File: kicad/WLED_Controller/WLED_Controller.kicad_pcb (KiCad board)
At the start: 2 copper layers, 72 x 50 mm, 51 parts, among them J1 USB_C_Receptacle_USB2.0, J3 AudioJack, Q1 BC847, Q2 BC847, SW1 SW_RESET, SW2 SW_BOOT, SW3 SW_Push, SW4 SW_Push, SW5 SW_Push, SW6 SW_Push, SW7 SW_Push, U1 ESP32-WROOM-32, U2 CH340C, U3 NCP1117-3.3, U4 TSSP58P38

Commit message: begin creating schematic
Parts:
- removed C13, C14, C15, C16: 100n, Capacitor_SMD:C_0603_1608Metric_Pad1.08x0.95mm_HandSolder
- removed SW4, SW5, SW6, SW7: SW_Push, Button_Switch_THT:SW_PUSH_6mm_H13mm
- added J2: Conn_01x05, GioN_Custom:TerminalBlock_WAGO_236-405_1x05_P5.00mm_45Degree, F.Cu at (19.5, -9.40)
- added J5: Conn_01x05, GioN_Custom:TerminalBlock_WAGO_236-405_1x05_P5.00mm_45Degree, F.Cu at (9.40, -31.6)
- added J6: Conn_01x02, GioN_Custom:TerminalBlock_WAGO_236-402_1x02_P5.00mm_45Degree, F.Cu at (36.6, -40.6)
- added JP1: SolderJumper_3_Open, Jumper:SolderJumper-3_P1.3mm_Open_RoundedPad1.0x1.5mm_NumberLabels, F.Cu at (11.4, -5.59)
- added JP2: SolderJumper_2_Open, Jumper:SolderJumper-2_P1.3mm_Open_RoundedPad1.0x1.5mm, F.Cu at (28.6, -24.1)
- added JP3: SolderJumper_2_Open, Jumper:SolderJumper-2_P1.3mm_Open_RoundedPad1.0x1.5mm, F.Cu at (24.9, -16.5)
- added JP4: SolderJumper_3_Open, Jumper:SolderJumper-3_P1.3mm_Open_RoundedPad1.0x1.5mm_NumberLabels, F.Cu at (45.5, -11.2)
- added Q10: IRFL4105PBF, Package_TO_SOT_SMD:SOT-223, B.Cu at (38.4, -19.3)
- added Q3: IRFL4105PBF, Package_TO_SOT_SMD:SOT-223, B.Cu at (16.3, -19.3)
- added Q4: IRFL4105PBF, Package_TO_SOT_SMD:SOT-223, F.Cu at (18.8, -30.5)
- added Q5: IRFL4105PBF, Package_TO_SOT_SMD:SOT-223, F.Cu at (26.2, -30.5)
- added Q6: IRFL4105PBF, Package_TO_SOT_SMD:SOT-223, F.Cu at (33.5, -30.5)
- added Q7: IRFL4105PBF, Package_TO_SOT_SMD:SOT-223, F.Cu at (40.9, -30.5)
- added Q8: IRFL4105PBF, Package_TO_SOT_SMD:SOT-223, B.Cu at (23.6, -19.3)
- added Q9: IRFL4105PBF, Package_TO_SOT_SMD:SOT-223, B.Cu at (31.0, -19.3)
- added R13: 100R, Resistor_SMD:R_0603_1608Metric_Pad0.98x0.95mm_HandSolder, F.Cu at (11.4, 36.2)
- added R14: 100R, Resistor_SMD:R_0603_1608Metric_Pad0.98x0.95mm_HandSolder, F.Cu at (11.4, 38.7)
- added R16: 10k, Resistor_SMD:R_0603_1608Metric_Pad0.98x0.95mm_HandSolder, F.Cu at (11.4, 43.7)
- added R18: 10k, Resistor_SMD:R_0603_1608Metric_Pad0.98x0.95mm_HandSolder, F.Cu at (11.4, 48.7)
- added R20: 10k, Resistor_SMD:R_0603_1608Metric_Pad0.98x0.95mm_HandSolder, F.Cu at (15.7, 38.7)
- added R22: 10k, Resistor_SMD:R_0603_1608Metric_Pad0.98x0.95mm_HandSolder, F.Cu at (15.7, 43.7)
- added R23: 100R, Resistor_SMD:R_0603_1608Metric_Pad0.98x0.95mm_HandSolder, F.Cu at (15.7, 46.2)
- added R24: 100R, Resistor_SMD:R_0603_1608Metric_Pad0.98x0.95mm_HandSolder, F.Cu at (15.7, 48.7)
- added R25: 10k, Resistor_SMD:R_0603_1608Metric_Pad0.98x0.95mm_HandSolder, F.Cu at (20.1, 36.2)
- added R26: 10k, Resistor_SMD:R_0603_1608Metric_Pad0.98x0.95mm_HandSolder, F.Cu at (20.1, 38.7)
- added R27: 10k, Resistor_SMD:R_0603_1608Metric_Pad0.98x0.95mm_HandSolder, F.Cu at (20.1, 41.2)
- added R28: 10k, Resistor_SMD:R_0603_1608Metric_Pad0.98x0.95mm_HandSolder, F.Cu at (20.1, 43.7)
- R15, R17, R19, R21: value 10k -> 100R
- U2: moved to B.Cu
- moved C10 172.5 mm to (51.6, -43.1), turned to -90 degrees
- moved C11 170.8 mm to (49.3, -40.1)
- moved U3 169.2 mm to (56.1, -45.2), turned to 90 degrees
- moved C6 163.6 mm to (56.1, -37.8), turned to 180 degrees
- moved C7 161.2 mm to (56.1, -39.9), turned to 180 degrees
- moved C3 160.5 mm to (63.5, -39.9)
- moved SW1 156.9 mm to (63.2, -46.2), turned to -90 degrees
- moved C2 155.2 mm to (63.5, -37.6)
- moved C1 148.4 mm to (64.2, -35.6)
- moved SW3 146.6 mm to (42.5, -48.5)
- moved U4 139.3 mm to (69.9, -37.6), turned to 90 degrees
- moved D4 137.4 mm to (64.0, -2.40), turned to 90 degrees
- moved R11 136.7 mm to (64.0, -12.3), turned to -90 degrees
- moved R8 130.2 mm to (59.9, -12.3), turned to 90 degrees
- moved U2 128.5 mm to (55.8, -14.3), turned to 90 degrees
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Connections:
- net Button1 renamed Button0
- net CS renamed IO5
- net DTA/CTRL renamed IO25
- net MOSI renamed IO23
- net ON renamed IO22
- net RESET renamed IO4
- net SCLK renamed IO18
- net SENSE2 renamed IO26
- J3 pad 2: SENSE1 -> SENSE0
- R15 pad 1: +3.3V -> R1
- R15 pad 2: Button2 -> Net-(Q4-G)
- R17 pad 1: +3.3V -> G1
- R17 pad 2: Button3 -> Net-(Q5-G)
- R19 pad 1: +3.3V -> B1
- R19 pad 2: Button4 -> Net-(Q6-G)
- R21 pad 1: +3.3V -> W1
- R21 pad 2: Button5 -> Net-(Q7-G)
- U1 pad 13: SENSE1 -> IO14
- U1 pad 14: unconnected-(U1-IO12-Pad14) -> IO12
- U1 pad 16: Button5 -> IO13
- U1 pad 23: Button4 -> IO15
- U1 pad 27: Button3 -> IO16
- U1 pad 28: Button2 -> IO17
- U1 pad 33: unconnected-(U1-IO21-Pad33) -> IO21
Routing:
- net Net-(JP1-B): track 0.00 -> 46.8 mm
- net Net-(J5-Pin_4): track 0.00 -> 31.3 mm
- net Net-(J2-Pin_3): track 0.00 -> 23.8 mm
- net Net-(J5-Pin_3): track 0.00 -> 22.8 mm
- net Net-(J5-Pin_2): track 0.00 -> 17.2 mm
- net Net-(J2-Pin_2): track 0.00 -> 17.0 mm
- net Net-(J2-Pin_4): track 0.00 -> 13.2 mm
- net Net-(J5-Pin_5): track 0.00 -> 12.6 mm
- net Net-(J2-Pin_5): track 0.00 -> 11.7 mm
- net Net-(JP4-B): track 0.00 -> 10.7 mm, vias 0 -> 1

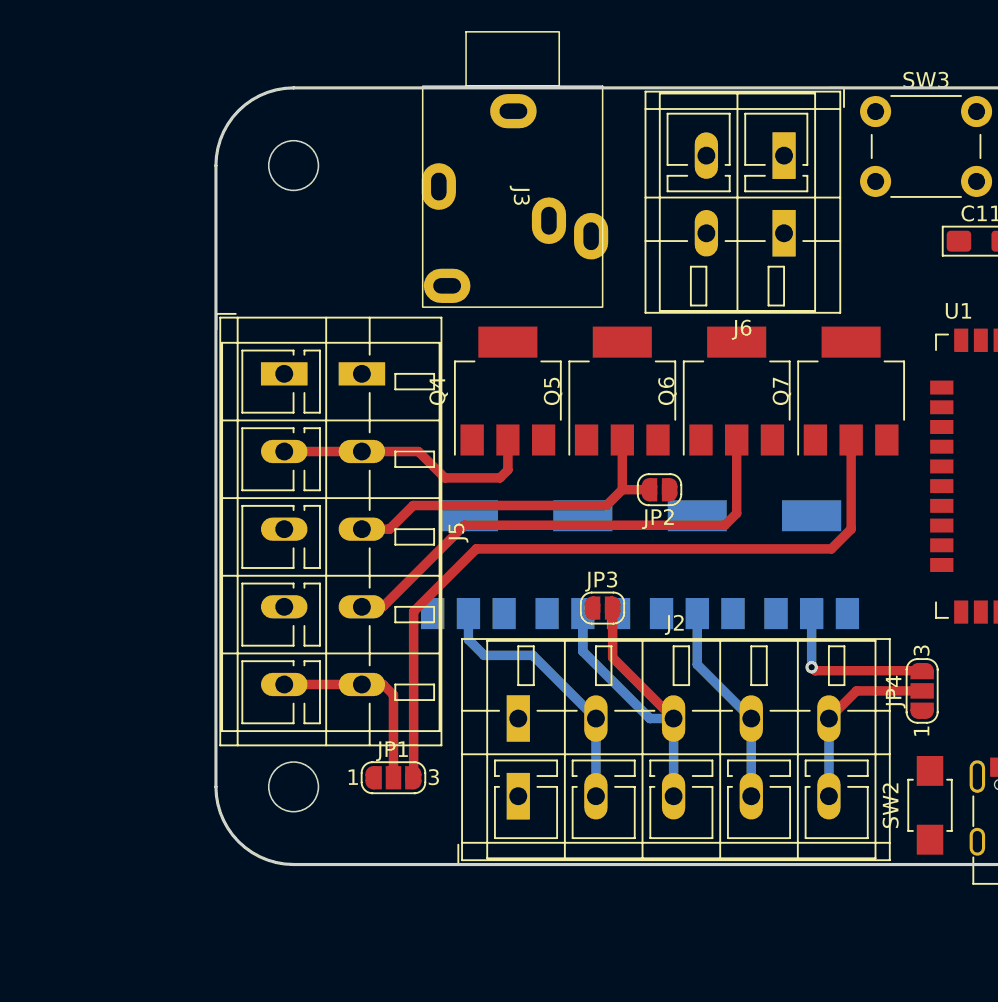
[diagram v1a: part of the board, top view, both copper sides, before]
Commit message: add Microphone
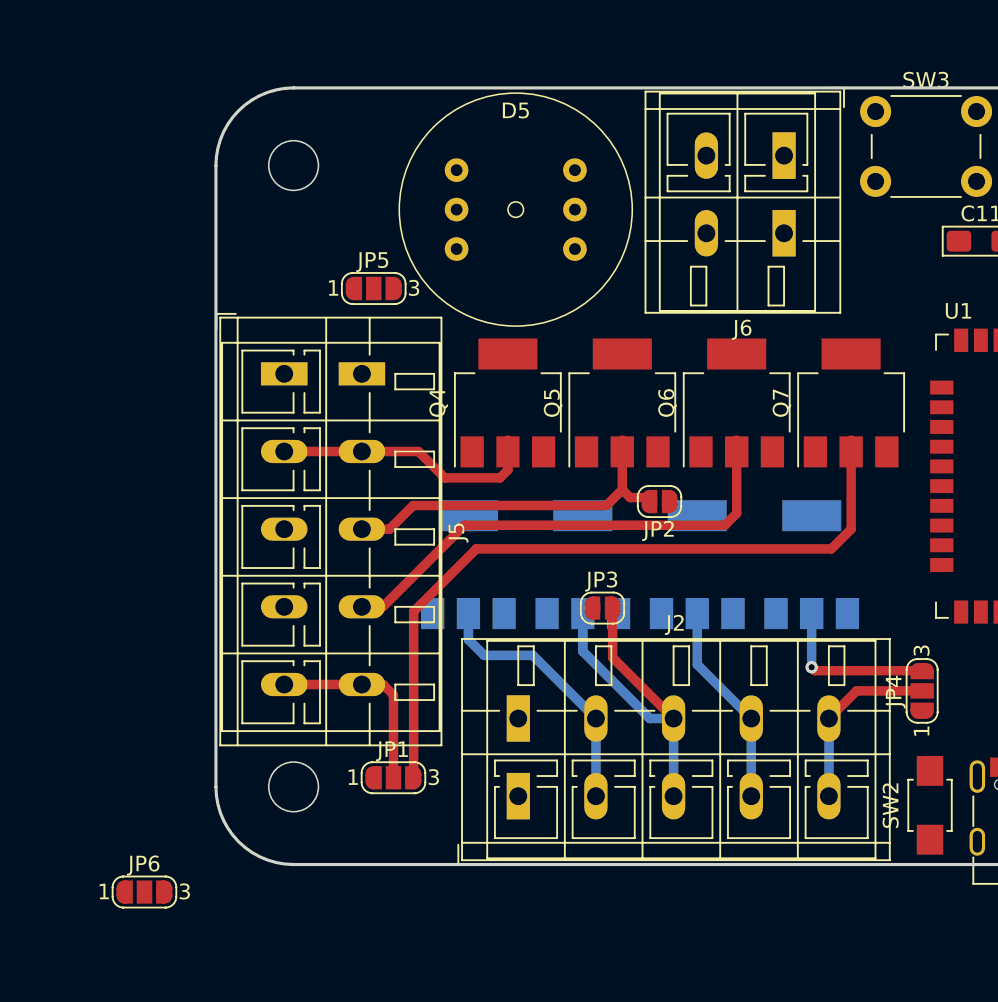
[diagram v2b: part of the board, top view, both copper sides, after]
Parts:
- removed J3: AudioJack, GioN_Custom:PG-203JN
- added D5: INMP441, GioN_Custom:INMP441_Module, F.Cu at (19.3, -42.2)
- added JP5: SolderJumper_3_Open, Jumper:SolderJumper-3_P1.3mm_Open_RoundedPad1.0x1.5mm_NumberLabels, F.Cu at (10.2, -37.1)
- added JP6: SolderJumper_3_Open, Jumper:SolderJumper-3_P1.3mm_Open_RoundedPad1.0x1.5mm_NumberLabels, F.Cu at (-4.60, 1.77)
- moved JP2 0.76 mm to (28.6, -23.4)
- moved Q4 0.76 mm to (18.8, -29.7)
- moved Q5 0.76 mm to (26.2, -29.7)
- moved Q6 0.76 mm to (33.5, -29.7)
- moved Q7 0.76 mm to (40.9, -29.7)
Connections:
- J2 pad 1: +24V -> Net-(J2-Pin_1)
- J5 pad 1: +24V -> Net-(J5-Pin_1)
- U1 pad 11: IO26 -> MIC_SD
- U1 pad 29: IO5 -> MIC_WS
- U1 pad 33: IO21 -> MIC_SCK
- U4 pad 1: Net-(U4-OUT) -> SENSE0

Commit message: Add V1
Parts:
- removed J5: Conn_01x05, GioN_Custom:TerminalBlock_WAGO_236-405_1x05_P5.00mm_45Degree
- removed JP1, JP4, JP5, JP6: SolderJumper_3_Open, Jumper:SolderJumper-3_P1.3mm_Open_RoundedPad1.0x1.5mm_NumberLabels
- removed JP2, JP3: SolderJumper_2_Open, Jumper:SolderJumper-2_P1.3mm_Open_RoundedPad1.0x1.5mm
- removed Q10, Q3, Q4, Q5, Q6, Q7, Q8, Q9: IRFL4105PBF, Package_TO_SOT_SMD:SOT-223
- removed R13, R14, R15, R17, R19, R21, R23, R24: 100R, Resistor_SMD:R_0603_1608Metric_Pad0.98x0.95mm_HandSolder
- removed R16, R18, R20, R22, R25, R26, R27, R28: 10k, Resistor_SMD:R_0603_1608Metric_Pad0.98x0.95mm_HandSolder
- added C13: 100n, Capacitor_SMD:C_0603_1608Metric_Pad1.08x0.95mm_HandSolder, F.Cu at (26.3, -20.3)
- added J3: Conn_01x03, GioN_Custom:TerminalBlock_WAGO_236-403_1x03_P5.00mm_45Degree, F.Cu at (30.9, -9.65)
- added J4: Conn_01x03, GioN_Custom:TerminalBlock_WAGO_236-403_1x03_P5.00mm_45Degree, F.Cu at (12.4, -9.65)
- added U5: 74HC14, Package_SO:SOIC-14_3.9x8.7mm_P1.27mm, F.Cu at (27.8, -25.9)
- C5, Q1, Q2, R10, R4, R9: moved to B.Cu
- J2: value Conn_01x05 -> Conn_01x03; footprint GioN_Custom:TerminalBlock_WAGO_236-405_1x05_P5.00mm_45Degree -> GioN_Custom:TerminalBlock_WAGO_236-403_1x03_P5.00mm_45Degree
- moved R2 102.1 mm to (55.5, -12.4), turned to 180 degrees
- moved R1 99.9 mm to (55.5, -14.2), turned to 180 degrees
- moved D2 93.2 mm to (51.8, -12.4), turned to 180 degrees
- moved D1 92.7 mm to (51.8, -14.2), turned to 180 degrees
- moved C12 75.5 mm to (32.5, -26.3), turned to -90 degrees
- moved R4 72.8 mm to (59.2, -31.0), turned to 90 degrees
- moved C8 72.1 mm to (60.2, -35.6)
- moved C4 70.7 mm to (44.3, -39.9), turned to 180 degrees
- moved R12 69.8 mm to (43.9, -26.2), turned to -90 degrees
- moved R6 68.1 mm to (42.8, -18.0)
- moved Q2 63.3 mm to (49.4, -24.6), turned to 180 degrees
- moved R10 58.9 mm to (53.6, -22.9), turned to 90 degrees
- moved C9 57.9 mm to (42.8, -16.3)
- moved R9 56.9 mm to (52.1, -22.9), turned to -90 degrees
- moved Q1 56.2 mm to (49.4, -21.1), turned to 180 degrees
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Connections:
- J1 pad A5: unconnected-(J1-CC1-PadA5) -> Net-(J1-CC1)
- J1 pad A8: Net-(J1-SBU1) -> unconnected-(J1-SBU1-PadA8)
- J1 pad B5: unconnected-(J1-CC2-PadB5) -> Net-(J1-CC2)
- J1 pad B8: Net-(J1-SBU2) -> unconnected-(J1-SBU2-PadB8)
- J2 pad 1: Net-(J2-Pin_1) -> +5V
- J2 pad 3: Net-(J2-Pin_3) -> GND
- J6 pad 1: +24V -> +5V
- R3 pad 1: Net-(J1-SBU2) -> Net-(J1-CC2)
- R5 pad 1: Net-(J1-SBU1) -> Net-(J1-CC1)
- U1 pad 23: IO15 -> LED0
- U1 pad 27: IO16 -> LED1
- U1 pad 28: IO17 -> LED2
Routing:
- net +5V: track 0.00 -> 195.3 mm, vias 0 -> 2
- net +3.3V: track 0.00 -> 166.3 mm, vias 0 -> 2
- net MIC_WS: track 0.00 -> 60.1 mm, vias 0 -> 1
- net MIC_SCK: track 0.00 -> 58.0 mm, vias 0 -> 1
- net ESP_EN: track 0.00 -> 49.7 mm, vias 0 -> 2
- net Net-(JP1-B): track 46.8 -> 0.00 mm
- net LED1: track 0.00 -> 45.6 mm, vias 0 -> 2
- net Button0: track 0.00 -> 41.5 mm, vias 0 -> 1
- net LED2: track 0.00 -> 35.5 mm, vias 0 -> 2
- net MIC_SD: track 0.00 -> 34.3 mm, vias 0 -> 1
- net Net-(J5-Pin_4): track 31.3 -> 0.00 mm
- net Net-(J4-Pin_2): track 0.00 -> 27.2 mm
- net Net-(J3-Pin_2): track 0.00 -> 25.8 mm
- net Net-(J2-Pin_3): track 23.8 -> 0.00 mm
- net Net-(J5-Pin_3): track 23.1 -> 0.00 mm
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- added copper zone on B.Cu, net GND
- added copper zone on F.Cu, net GND
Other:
- board text added: "+5V"
- board text added: "BOOT"
- board text added: "GND"
- board text added: "IO15 LED0"
- board text added: "IO16 LED1"
- board text added: "IO17 LED2"
- board text added: "IO19 BTN0"
- board text added: "IO27 REM"
- board text added: "RST"
- board text added: "WLED Controller V1 02/2024 Gioulekas Nikos"
- board text added: "WS: IO05 SCK: IO21 SD: IO26"
- board text added: "bot"
- board text added: "top"
